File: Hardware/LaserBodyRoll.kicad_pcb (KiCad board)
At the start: 2 copper layers, 104 x 40 mm, 93 parts, among them J1 CONN_01X02, J2 FTSH-105-01-L-DV-K, J3 Conn_01x04, J4 Conn_01x04, J5 CONN_01X02, J6 CONN_01X02, J8 Raspberry_Pi_2_3, Q1 Q_NPN_BCE, Q2 Q_NPN_BCE, Q3 Q_NPN_BCE, Q4 Q_NPN_BCE, U1 TPS821XX, U2 CY8C4A25LQI-473, U3 LMC6032, U5 ICM-20602, U6 VL53L0X, U7 STLM75

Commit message: Worked on initial placement.
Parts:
- removed D10, D11, D12, D15, D9: D_TVS, Diodes_SMD:D_SMB
- removed D8: D_Zener, Diodes_SMD:D_SMB
- removed J1, J5, J6: CONN_01X02, Pin_Headers:Pin_Header_Straight_1x02_Pitch2.54mm
- removed J8: Raspberry_Pi_2_3, Pin_Headers:Pin_Header_Straight_2x20_Pitch2.54mm
- removed Q2, Q3, Q4: Q_NPN_BCE, TO_SOT_Packages_SMD:SOT-23
- removed R27: 24.3k, Resistors_SMD:R_0603
- removed R28: 75k, Resistors_SMD:R_0603
- removed R29, R30: 30k, Resistors_SMD:R_0805
- removed R31, R32: 1.7k, Resistors_SMD:R_0603
- removed R33, R34: 10k, Resistors_SMD:R_0603
- removed R35, R36, R37: 330, Resistors_SMD:R_0603
- removed TP5: Test_Point, Connectors_TestPoints:Test_Point_Pad_d2.0mm
- removed W14: TEST_1P, Connectors_TestPoints:Test_Point_Pad_d2.0mm
- added C15: 100n, Capacitors_SMD:C_0603, F.Cu at (97.0, 50.0)
- added C23: 1u, Capacitors_SMD:C_0603_HandSoldering, F.Cu at (91.0, 39.0)
- added C24: 0.1u, Capacitors_SMD:C_0603, F.Cu at (102.0, 51.0)
- added C25: 2.2U, Capacitors_SMD:C_0603, F.Cu at (106.0, 63.0)
- added C26: 10n, Capacitors_SMD:C_0603, F.Cu at (103.0, 61.0)
- added C27: 4.7u, Capacitors_SMD:C_0603, F.Cu at (102.0, 53.0)
- added C8: 6.8, Capacitors_SMD:C_0603, F.Cu at (75.0, 47.0)
- added L1: L_Core_Ferrite, Inductors_SMD:L_0805, F.Cu at (111.0, 70.0)
- added U10: VL53L0X, KicadFootprint:VL53L0x, F.Cu at (103.0, 55.8)
- added U4: LMC6032, SMD_Packages:SOIC-8-N, F.Cu at (65.0, 58.0)
- added U8: ICM-20602, KicadFootprint:QFN-16-no_center_3x3mm_Pitch0.5mm, F.Cu at (103.0, 67.0)
- added U9: W25Qxx, Housings_SOIC:SOIC-8_3.9x4.9mm_Pitch1.27mm, F.Cu at (91.0, 45.0)
- added W1: TEST_1P, Connectors_TestPoints:Test_Point_Pad_d2.0mm, F.Cu at (47.0, 50.0)
- added Y1: 8MHz, Crystals:Crystal_SMD_MicroCrystal_CC4V-T1A-2pin_5.0x1.9mm_HandSoldering, F.Cu at (74.0, 57.0)
- added Y2: 32.768, Crystals:Crystal_SMD_MicroCrystal_CC7V-T1A-2pin_3.2x1.5mm_HandSoldering, F.Cu at (73.0, 50.0)
- C1: value 0.1u -> 10u
- C10: value 0.1u -> 1.5F
- C11: value .01u -> 4.7u
- C12, C13, C14: value .01u -> 100n
- C17: value 0.1u -> 10n
- C18: value 2.2U -> 10n
- C19: value 100n -> 10n
- C2: value 0.1u -> 3.3n
- C20: value 10n -> 0.1n
- C21: value 4.7u -> 0.1u; footprint Capacitors_SMD:C_0603 -> Capacitors_SMD:C_0603_HandSoldering
- C22: footprint Capacitors_SMD:C_0603 -> Capacitors_SMD:C_0603_HandSoldering
- C3: value 1u -> 22u; footprint Capacitors_SMD:C_0603 -> SMD_Packages:SMD-1210_Pol
- C4: value 10u -> 1u; footprint Capacitors_SMD:C_0805 -> Capacitors_SMD:C_0603
- C5: value 3.3n -> 2.2U; footprint Capacitors_SMD:C_0805 -> Capacitors_SMD:C_0603
- C6: value 0.1u -> 20p
- C7: value 22u -> 20p; footprint SMD_Packages:SMD-1210_Pol -> Capacitors_SMD:C_0603
- C9: value 1u -> 6.8
- D2: value D_Zener -> D_TVS; footprint Diodes_SMD:D_SOD-123 -> Diodes_SMD:D_SMB
- D3: value D_Zener -> D
- D4, D5: footprint Diodes_SMD:D_SOD-123 -> Diodes_SMD:D_SMB
- D6: value LED_RABG -> D_TVS; footprint KicadFootprint:CREE_PLCC4 -> Diodes_SMD:D_SMB
- D7: value D_Zener -> LED_RABG; footprint Diodes_SMD:D_SMB -> KicadFootprint:CREE_PLCC4
- J3: value Conn_01x04 -> FTSH-105-01-L-DV-K; footprint Pin_Headers:Pin_Header_Straight_1x04_Pitch2.54mm -> KicadFootprint:FTSH-105-01-L-DV-K
- J4: value Conn_01x04 -> Conn_01x08; footprint Pin_Headers:Pin_Header_Straight_1x04_Pitch2.54mm -> Pin_Headers:Pin_Header_Straight_1x08_Pitch2.54mm
- R1: value 10k -> 525k
- R10: value 24.3k -> 75k
- R11, R12: value DNI -> 24.3k
- R2: value 10k -> 100k
- R20, R22: value 24.3k -> 330
- R21: value 75k -> 330
- R23, R24: value 24.3k -> 1.7k
- R25, R26, R9: value 24.3k -> 10k
- R3: value 100k -> 360; footprint Resistors_SMD:R_0805 -> Resistors_SMD:R_0603
- R4: value 525k -> 120; footprint Resistors_SMD:R_0805 -> Resistors_SMD:R_0603
- R5, R6: value 24.3k -> 0
- R7, R8: value DNI -> 0
- U2: value CY8C4A25LQI-473 -> LDK130-ADJ_SOT23_SOT353; footprint Housings_DFN_QFN:UQFN-48-1EP_6x6mm_Pitch0.4mm -> TO_SOT_Packages_SMD:SOT-353_SC-70-5
- U3: value LMC6032 -> STM32F303RETx; footprint SMD_Packages:SOIC-8-N -> Housings_QFP:TQFP-64_10x10mm_Pitch0.5mm
- U5: value ICM-20602 -> ITS42K5D; footprint KicadFootprint:QFN-16-no_center_3x3mm_Pitch0.5mm -> KicadFootprint:PG-TSON-10
- U6: value VL53L0X -> CYBLE-022001-00; footprint KicadFootprint:VL53L0x -> KicadFootprint:CYBLE-022001
- U7: value STLM75 -> TJA1051T-3; footprint Housings_SSOP:TSSOP-8_3x3mm_Pitch0.65mm -> Housings_SOIC:SOIC-8_3.9x4.9mm_Pitch1.27mm
- moved J4 102.1 mm to (40.0, 51.6), turned to 0 degrees
- moved R18 81.6 mm to (45.0, 71.0), turned to 0 degrees
- moved R15 79.4 mm to (44.0, 57.0), turned to 0 degrees
- moved R16 78.8 mm to (44.0, 59.0), turned to 0 degrees
- moved R19 73.2 mm to (49.0, 71.0), turned to 0 degrees
- moved Q1 72.9 mm to (54.0, 76.0)
- moved R17 67.1 mm to (55.0, 71.0), turned to 0 degrees
- moved TP2 66.8 mm to (115.0, 60.0)
- moved D5 66.2 mm to (50.0, 55.0), turned to 0 degrees
- moved D2 63.5 mm to (45.0, 44.0), turned to 270 degrees
- moved D4 61.8 mm to (50.0, 61.0), turned to 0 degrees
- moved J2 51.9 mm to (102.0, 43.5)
- moved R20 50.7 mm to (81.0, 74.0), turned to 0 degrees
- moved TP3 48.1 mm to (109.0, 46.0)
- moved TP1 48.0 mm to (96.0, 39.0)
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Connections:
- C1 pad 1: VCC -> 12V
- C11 pad 1: Net-(C11-Pad1) -> VCC
- C12 pad 1: Net-(C12-Pad1) -> VCC
- C13 pad 1: Net-(C13-Pad1) -> VCC
- C14 pad 1: Net-(C14-Pad1) -> VCC
- C16 pad 1: Net-(C16-Pad1) -> VCC
- C18 pad 1: VCC -> Net-(C18-Pad1)
- C19 pad 1: VCC -> Net-(C19-Pad1)
- C2 pad 1: VCC -> Net-(C2-Pad1)
- C21 pad 1: VCC -> Net-(C21-Pad1)
- C3 pad 1: VCC -> 5V
- C4 pad 1: /IO/12V -> 5V
- C5 pad 1: Net-(C5-Pad1) -> VCC
- C7 pad 1: +5V -> Net-(C7-Pad1)
- C9 pad 1: VCC -> Net-(C9-Pad1)
- D1 pad 1: /IO/12V -> 12V
- D1 pad 2: Net-(D1-Pad2) -> PWR_IN
- D2 pad 1: VCC -> 12V
- D2 pad 2: Net-(C11-Pad1) -> GND
- D3 pad 1: Net-(C11-Pad1) -> Net-(C10-Pad1)
- D3 pad 2: GND -> VCC
- D4 pad 1: VCC -> Net-(C18-Pad1)
- D4 pad 2: Net-(C12-Pad1) -> GND
- D5 pad 1: Net-(C12-Pad1) -> Net-(C19-Pad1)
- D6 pad 1: Net-(D6-Pad1) -> /IO/DIN
- D6 pad 2: VCC -> GND
- D7 pad 1: Net-(C13-Pad1) -> Net-(D7-Pad1)
- D7 pad 2: GND -> VCC
- J2 pad 10: /Processor/XRES -> /Processor/STM_RES
- J2 pad 2: /Processor/SWDIO -> /Processor/STM_SWDIO
- J2 pad 4: /Processor/SWDCLK -> /Processor/STM_SWDCLK
- J3 pad 1: /IO/ANA_OUT1 -> VCC
- J3 pad 2: /IO/ANA_OUT2 -> /Logic/SWDIO
- J3 pad 3: /IO/ANA_IN1 -> GND
- J3 pad 4: /IO/ANA_IN2 -> /Logic/SWDCLK
- J4 pad 1: /IO/DOUT1 -> PWR_IN
- J4 pad 2: /IO/DOUT2 -> GND
- J4 pad 3: /IO/DIN1 -> /IO/ANA_OUT1
- J4 pad 4: /IO/DIN2 -> /IO/ANA_OUT2
- Q1 pad 2: Net-(Q1-Pad2) -> GND
- Q1 pad 3: GND -> CPU_DIN1
- R1 pad 1: Net-(R1-Pad1) -> 5V
- R1 pad 2: GND -> Net-(R1-Pad2)
- R10 pad 1: /IO/CPU_ANA_IN2 -> 12V
- R10 pad 2: Net-(C12-Pad1) -> Net-(R10-Pad2)
- R11 pad 1: Net-(C13-Pad1) -> Net-(R11-Pad1)
- R11 pad 2: /IO/CPU_ANA_OUT2 -> GND
- R12 pad 1: Net-(C14-Pad1) -> Net-(R12-Pad1)
- R12 pad 2: /IO/CPU_ANA_OUT1 -> GND
- R13 pad 1: /IO/ANA_OUT1 -> Net-(R12-Pad1)
- R13 pad 2: Net-(C14-Pad1) -> Net-(C18-Pad1)
- R14 pad 1: /IO/ANA_OUT2 -> Net-(R11-Pad1)
- R14 pad 2: Net-(C13-Pad1) -> Net-(C19-Pad1)
- R15 pad 1: Net-(Q1-Pad1) -> /IO/ANA_OUT1
- R15 pad 2: /IO/CPU_DOUT1 -> Net-(C19-Pad1)
- R16 pad 1: /IO/DIN1 -> /IO/ANA_OUT2
- R16 pad 2: Net-(J5-Pad2) -> Net-(C18-Pad1)
- R17 pad 1: Net-(Q1-Pad2) -> /IO/DIN
- R17 pad 2: /IO/12V -> /IO/12V_PULLUP
- R18 pad 1: /IO/DIN1 -> /IO/DIN
- R18 pad 2: Net-(Q2-Pad1) -> Net-(Q1-Pad1)
- R19 pad 1: /IO/DOUT1 -> Net-(Q1-Pad1)
- R19 pad 2: Net-(Q1-Pad2) -> GND
- R2 pad 1: Net-(R2-Pad1) -> Net-(R1-Pad2)
- R20 pad 1: Net-(Q2-Pad1) -> Net-(D7-Pad1)
- R20 pad 2: GND -> RED
- R21 pad 1: VCC -> Net-(D7-Pad4)
- R21 pad 2: /IO/CPU_DIN1 -> GREEN
- R22 pad 1: Net-(Q3-Pad1) -> Net-(D7-Pad3)
- R22 pad 2: /IO/CPU_DOUT2 -> BLUE
- R23 pad 1: /IO/DIN2 -> VCC
- R23 pad 2: Net-(J6-Pad2) -> SCL
- R24 pad 1: /IO/DIN2 -> VCC
- R24 pad 2: Net-(Q4-Pad1) -> SDA
- R25 pad 1: Net-(Q3-Pad2) -> VCC
- R25 pad 2: /IO/12V -> /Logic/VL53L0X_XSHUT
- R26 pad 1: /IO/DOUT2 -> VCC
- R26 pad 2: Net-(Q3-Pad2) -> /Logic/VL53L0X_GP
- R3 pad 1: Net-(R3-Pad1) -> VCC
- R3 pad 2: GND -> Net-(R3-Pad2)
- R4 pad 1: +5V -> Net-(R3-Pad2)
- R4 pad 2: Net-(R3-Pad1) -> GND
- R5 pad 1: Net-(C11-Pad1) -> Net-(R5-Pad1)
- R5 pad 2: /IO/ANA_IN1 -> Net-(C6-Pad1)
- R6 pad 1: Net-(C12-Pad1) -> Net-(R6-Pad1)
- R6 pad 2: /IO/ANA_IN2 -> Net-(C7-Pad1)
- R7 pad 1: GND -> Net-(R7-Pad1)
- R7 pad 2: Net-(C11-Pad1) -> Net-(C8-Pad1)
- R8 pad 1: GND -> Net-(R8-Pad1)
- R8 pad 2: Net-(C12-Pad1) -> Net-(C9-Pad1)
- R9 pad 1: /IO/CPU_ANA_IN1 -> GND
- R9 pad 2: Net-(C11-Pad1) -> Net-(R10-Pad2)
- TP1 pad 1: /Processor/XRES -> /Processor/STM_RES
- TP2 pad 1: +5V -> /Logic/XRES
- TP3 pad 1: VCC -> SCL
- TP4 pad 1: /Processor/SDA -> SDA
- U1 pad 1: /IO/12V -> 12V
- U1 pad 2: /IO/12V -> 12V
- U1 pad 4: +5V -> 5V
- U1 pad 5: +5V -> 5V
- U1 pad 6: Net-(R3-Pad1) -> Net-(R1-Pad2)
- U1 pad 8: Net-(C5-Pad1) -> Net-(C2-Pad1)
- U2 pad 1: Net-(U2-Pad1) -> 5V
- U2 pad 2: /IO/CPU_ANA_OUT2 -> GND
- U2 pad 3: /IO/CPU_ANA_OUT1 -> 5V
- U2 pad 4: /IO/CPU_DIN2 -> Net-(R3-Pad2)
- U2 pad 5: Net-(U2-Pad5) -> VCC
- U3 pad 1: Net-(C14-Pad1) -> Net-(C10-Pad1)
- U3 pad 2: Net-(R1-Pad1) -> Net-(U3-Pad2)
- U3 pad 3: /IO/CPU_ANA_OUT1 -> Net-(R7-Pad1)
- U3 pad 4: GND -> Net-(R8-Pad1)
- U3 pad 5: /IO/CPU_ANA_OUT2 -> Net-(R5-Pad1)
- U3 pad 6: Net-(R2-Pad1) -> Net-(R6-Pad1)
- U3 pad 7: Net-(C13-Pad1) -> /Processor/STM_RES
- U3 pad 8: /IO/12V -> CPU_DOUT1
- U5 pad 1: VCC -> CPU_DOUT1
- U5 pad 2: /Processor/SCL -> CPU_DOUT1_ST
- U5 pad 3: /Processor/SDA -> GND
- U5 pad 4: VCC -> CPU_DOUT2
- U5 pad 5: VCC -> CPU_DOUT2_ST
- U5 pad 6: /Processor/ICM_INT -> GND
- U5 pad 7: Net-(U5-Pad7) -> /IO/12V_PULLUP
- U5 pad 8: Net-(U5-Pad8) -> 12V
- U5 pad 9: GND -> /IO/DOUT
- U6 pad 1: VCC -> GND
- U6 pad 10: /Processor/SCL -> GND
- U6 pad 11: VCC -> /Logic/SWDIO
- U6 pad 12: GND -> BLE_SCLK
- U6 pad 2: GND -> Net-(U6-Pad2)
- U6 pad 3: GND -> Net-(U6-Pad3)
- U6 pad 4: GND -> Net-(U6-Pad4)
- U6 pad 5: /Processor/VL53L0X_XSHUT -> Net-(L1-Pad2)
- U6 pad 6: GND -> BLE_CS
- U6 pad 7: /Processor/VL53L0X_GP -> /Logic/SWDCLK
- U6 pad 9: /Processor/SDA -> Net-(U6-Pad9)
- U7 pad 1: /Processor/SDA -> CAN_TXD
- U7 pad 2: /Processor/SCL -> GND
- U7 pad 3: Net-(U7-Pad3) -> 5V
- U7 pad 4: GND -> CAN_RXD
- U7 pad 5: GND -> VCC
- U7 pad 6: GND -> CANL
- U7 pad 7: GND -> CANH
- U7 pad 8: VCC -> GND
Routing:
- net VCC: track 285.9 -> 0.00 mm, vias 16 -> 0
- net /IO/12V: track 175.7 -> 0.00 mm, vias 5 -> 0
- net /IO/CPU_DOUT2: track 89.7 -> 0.00 mm, vias 2 -> 0
- net /IO/CPU_ANA_IN2: track 82.8 -> 0.00 mm, vias 2 -> 0
- net /Processor/SCL: track 82.3 -> 0.00 mm, vias 7 -> 0
- net /Processor/SDA: track 80.8 -> 0.00 mm, vias 6 -> 0
- net /IO/CPU_ANA_IN1: track 77.8 -> 0.00 mm, vias 4 -> 0
- net /IO/CPU_DOUT1: track 76.1 -> 0.00 mm, vias 2 -> 0
- net /IO/CPU_DIN2: track 74.8 -> 0.00 mm, vias 2 -> 0
- net /IO/CPU_DIN1: track 63.9 -> 0.00 mm, vias 2 -> 0
- net /Processor/ICM_INT: track 56.6 -> 0.00 mm, vias 2 -> 0
- net /IO/CPU_ANA_OUT2: track 39.1 -> 0.00 mm, vias 2 -> 0
- net /Processor/SS: track 38.5 -> 0.00 mm, vias 1 -> 0
- net Net-(C14-Pad1): track 37.3 -> 0.00 mm
- net Net-(C13-Pad1): track 36.8 -> 0.00 mm, vias 3 -> 0
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- removed copper zone on B.Cu, net GND
- removed copper zone on F.Cu, net GND
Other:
- board outline removed
- board text removed: "+12V"
- board text removed: "AOUT1-AOUT2-AIN1-AIN2"
- board text removed: "DIN2 DIN1 DOUT2 DOUT1"
- board text removed: "GND"

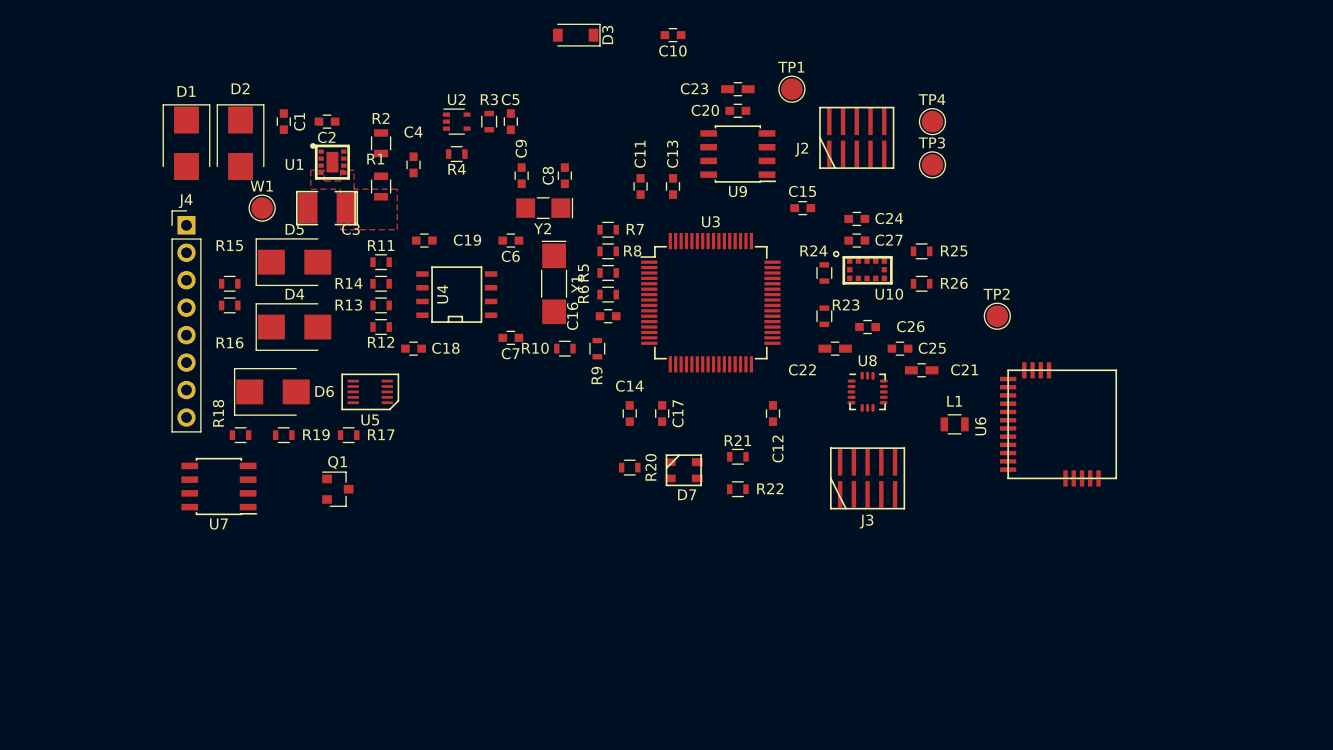
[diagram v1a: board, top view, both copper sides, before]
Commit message: Removed a bunch of old files. Created a board outline based on the Bud Box PN-1321-CMB
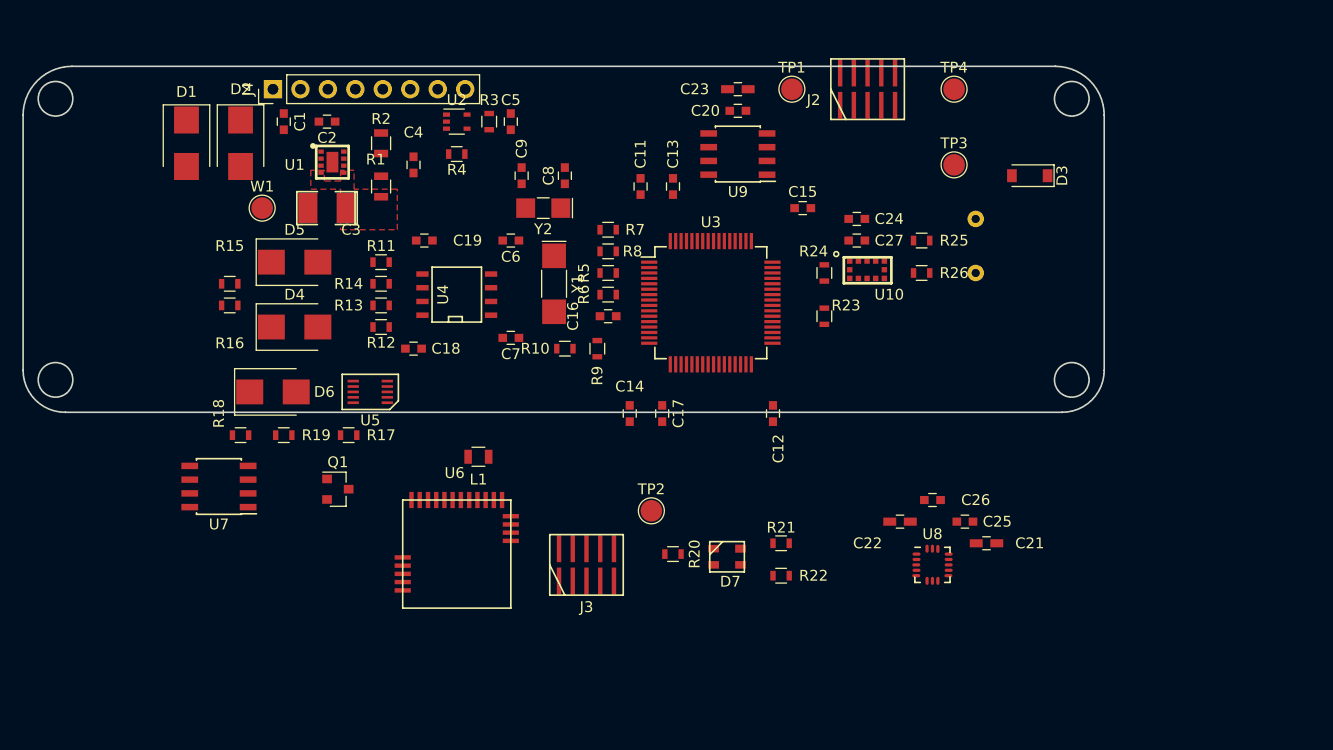
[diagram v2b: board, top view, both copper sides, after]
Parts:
- C10: footprint Capacitors_SMD:C_0603 -> KicadFootprint:Elna_Dynacap; moved to B.Cu
- moved U6 67.1 mm to (60.0, 87.0), turned to 180 degrees
- moved L1 44.2 mm to (67.0, 73.0), turned to 180 degrees
- moved D3 44.0 mm to (118.0, 47.0)
- moved TP2 36.7 mm to (83.0, 78.0)
- moved C10 35.6 mm to (113.0, 56.0), turned to 90 degrees
- moved J3 27.2 mm to (77.0, 83.0)
- moved C21 17.1 mm to (114.0, 81.0)
- moved C22 17.1 mm to (106.0, 79.0)
- moved C25 17.1 mm to (112.0, 79.0)
- moved C26 17.1 mm to (109.0, 77.0)
- moved U8 17.1 mm to (109.0, 83.0)
- moved J4 14.9 mm to (48.0, 39.0), turned to 90 degrees
- moved D7 8.94 mm to (90.0, 82.2)
- moved R20 8.94 mm to (85.0, 82.0)
- moved R21 8.94 mm to (95.0, 81.0)
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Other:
- board outline added: 100 x 32 mm

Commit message: Added a script to calculate current and charge time of the supercap.
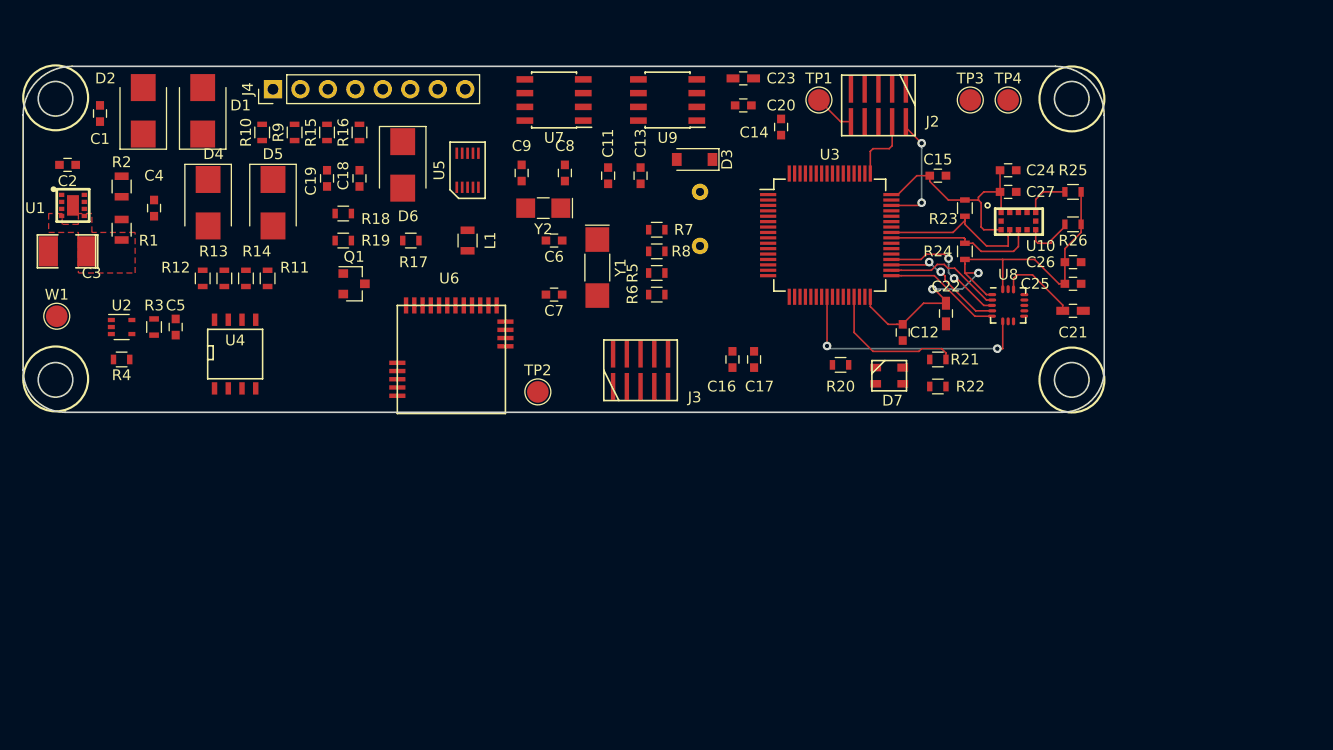
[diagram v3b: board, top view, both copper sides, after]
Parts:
- moved U7 47.3 mm to (74.0, 40.0)
- moved C5 36.4 mm to (39.0, 61.0)
- moved R3 36.4 mm to (37.0, 61.0)
- moved R4 36.4 mm to (34.0, 64.0)
- moved U2 36.4 mm to (34.0, 61.0)
- moved R10 34.4 mm to (47.0, 43.0), turned to 270 degrees
- moved R9 34.4 mm to (50.0, 43.0), turned to 270 degrees
- moved D3 31.0 mm to (87.0, 45.5)
- moved C14 30.0 mm to (95.0, 42.5), turned to 90 degrees
- moved C10 26.6 mm to (87.5, 48.5), turned to 270 degrees
- moved C26 25.6 mm to (122.0, 55.0)
- moved U8 25.0 mm to (116.0, 59.0)
- moved C2 24.3 mm to (29.0, 46.0)
- moved C3 24.3 mm to (29.0, 54.0)
- moved C4 24.3 mm to (37.0, 50.0)
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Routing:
- net VCC: track 0.00 -> 65.1 mm, vias 0 -> 2
- net IMU_INT: track 0.00 -> 23.6 mm, vias 0 -> 2
- net SCL: track 0.00 -> 14.8 mm
- net SDA: track 0.00 -> 14.2 mm
- net GREEN: track 0.00 -> 13.4 mm
- net IMU_MOSI: track 0.00 -> 12.2 mm, vias 0 -> 2
- net IMU_MISO: track 0.00 -> 11.5 mm, vias 0 -> 2
- net /Processor/STM_SWDIO: track 0.00 -> 11.0 mm, vias 0 -> 2
- net IMU_SCLK: track 0.00 -> 10.9 mm
- net IMU_CS: track 0.00 -> 10.9 mm
- net Net-(C21-Pad1): track 0.00 -> 7.40 mm
- net /Processor/STM_SWDCLK: track 0.00 -> 6.52 mm
- net /Logic/VL53L0X_GP: track 0.00 -> 4.85 mm
- net /Logic/VL53L0X_XSHUT: track 0.00 -> 4.19 mm
- net /Processor/STM_RES: track 0.00 -> 3.79 mm
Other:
- board text added: "LaserBodyRoll Rev C Copyright Nick Butts 2018"
- board text removed: "LaserBodyRoll Rev B Copyright Nick Butts 2017"

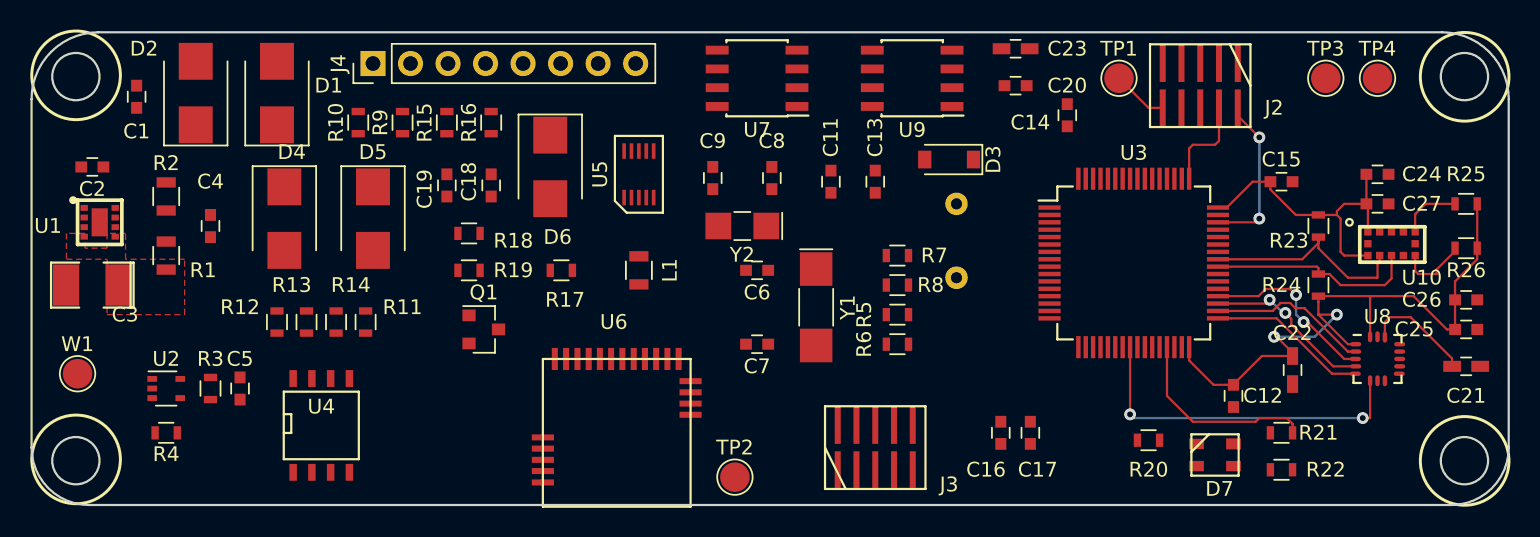
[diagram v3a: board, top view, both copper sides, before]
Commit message: Finished board. Added lots of stiching vias after reading a TI app note on EMC.
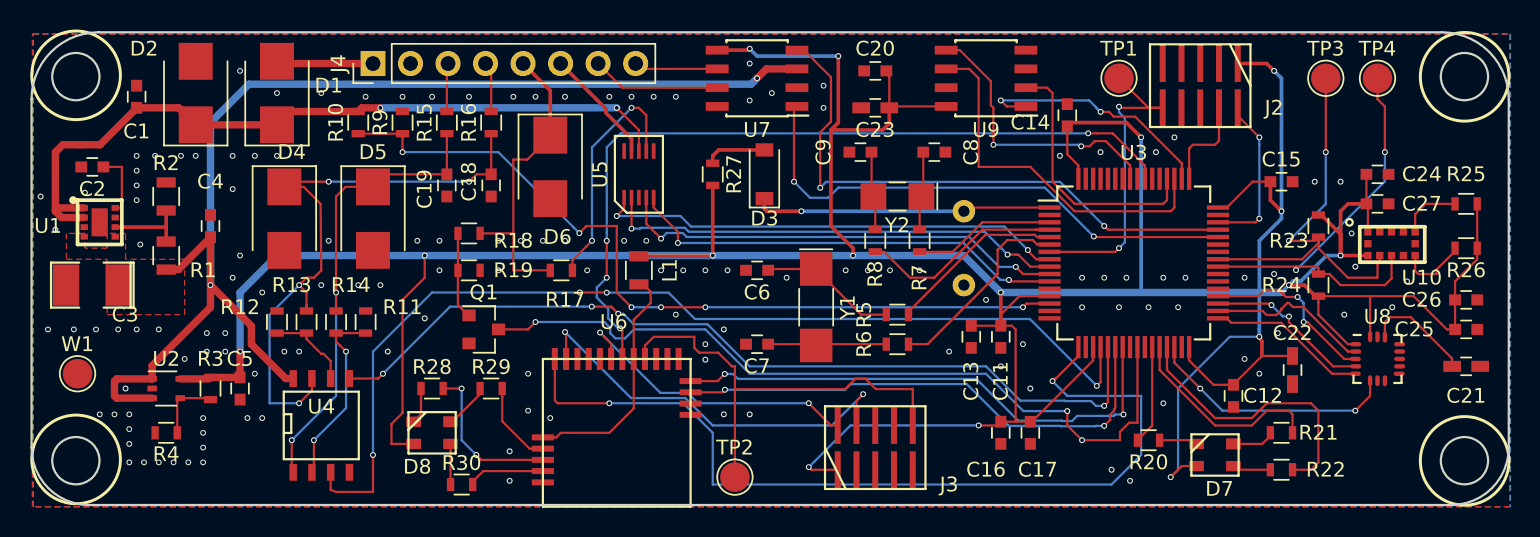
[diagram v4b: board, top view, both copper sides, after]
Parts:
- added D8: LED_RABG, KicadFootprint:CREE_PLCC4, F.Cu at (52.0, 64.0)
- added R27: 25, Resistors_SMD:R_0603, F.Cu at (71.0, 46.5)
- added R28: 330, Resistors_SMD:R_0603, F.Cu at (52.0, 61.0)
- added R29: 330, Resistors_SMD:R_0603, F.Cu at (56.0, 61.0)
- added R30: 330, Resistors_SMD:R_0603, F.Cu at (54.0, 67.5)
- moved C11 15.6 mm to (90.5, 57.5), turned to 270 degrees
- moved D3 12.5 mm to (74.5, 46.5), turned to 90 degrees
- moved C13 12.3 mm to (88.5, 57.5), turned to 270 degrees
- moved C8 11.1 mm to (86.0, 45.0), turned to 0 degrees
- moved Y2 10.7 mm to (83.5, 48.0)
- moved C23 10.3 mm to (82.0, 42.0), turned to 180 degrees
- moved C9 10.2 mm to (81.0, 45.0), turned to 180 degrees
- moved C20 9.55 mm to (82.0, 39.5), turned to 180 degrees
- moved U9 5.00 mm to (89.5, 40.0)
- moved R8 3.35 mm to (82.0, 51.0), turned to 90 degrees
- moved R7 1.80 mm to (85.0, 51.0), turned to 90 degrees
- moved C10 0.71 mm to (88.0, 49.0)
- turned R20 to 180 degrees
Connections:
- D3 pad 2: VCC -> Net-(D3-Pad2)
- J4 pad 5: /IO/DOUT -> /IO/DIN
- J4 pad 6: /IO/DIN -> /IO/DOUT
- U3 pad 24: IMU_INT -> Net-(U3-Pad24)
- U3 pad 27: Net-(U3-Pad27) -> RED
- U3 pad 28: BLUE -> GREEN
- U3 pad 29: GREEN -> BLUE
- U3 pad 30: RED -> IMU_INT
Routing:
- net VCC: track 65.1 -> 305.7 mm, vias 2 -> 16
- net 5V: track 0.00 -> 82.5 mm, vias 0 -> 2
- net DAC1: track 0.00 -> 69.6 mm, vias 0 -> 4
- net BLE_CS: track 0.00 -> 61.2 mm, vias 0 -> 2
- net DAC2: track 0.00 -> 60.0 mm, vias 0 -> 4
- net Net-(R10-Pad2): track 0.00 -> 55.5 mm, vias 0 -> 6
- net BLE_SCLK: track 0.00 -> 54.0 mm, vias 0 -> 4
- net CPU_DIN1: track 0.00 -> 54.0 mm, vias 0 -> 3
- net 12V: track 0.00 -> 51.9 mm, vias 0 -> 2
- net Net-(C18-Pad1): track 0.00 -> 41.7 mm, vias 0 -> 4
- net CAN_RXD: track 0.00 -> 39.3 mm, vias 0 -> 2
- net CAN_TXD: track 0.00 -> 36.0 mm, vias 0 -> 2
- net BLE_MOSI: track 0.00 -> 35.6 mm, vias 0 -> 2
- net BLE_MISO: track 0.00 -> 35.1 mm, vias 0 -> 2
- net Net-(C19-Pad1): track 0.00 -> 32.1 mm, vias 0 -> 2
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- added copper zone on F.Cu, net 5V
- added copper zone on B.Cu, net GND
- added copper zone on F.Cu, net GND
- removed copper zone on F.Cu, net +5V
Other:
- net class Default: via_dia 0.8 -> 0.4; via_drill 0.4 -> 0.254
- net class SmallVias added: clearance 0.2, trace_width 0.1524, via_dia 0.4, via_drill 0.254
- rule via_min_drill: 0.3 -> 0.254
- rule via_min_size: 0.4 -> 0.381
